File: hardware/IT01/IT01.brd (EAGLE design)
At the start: 23.5 x 23.5 mm, 11 parts

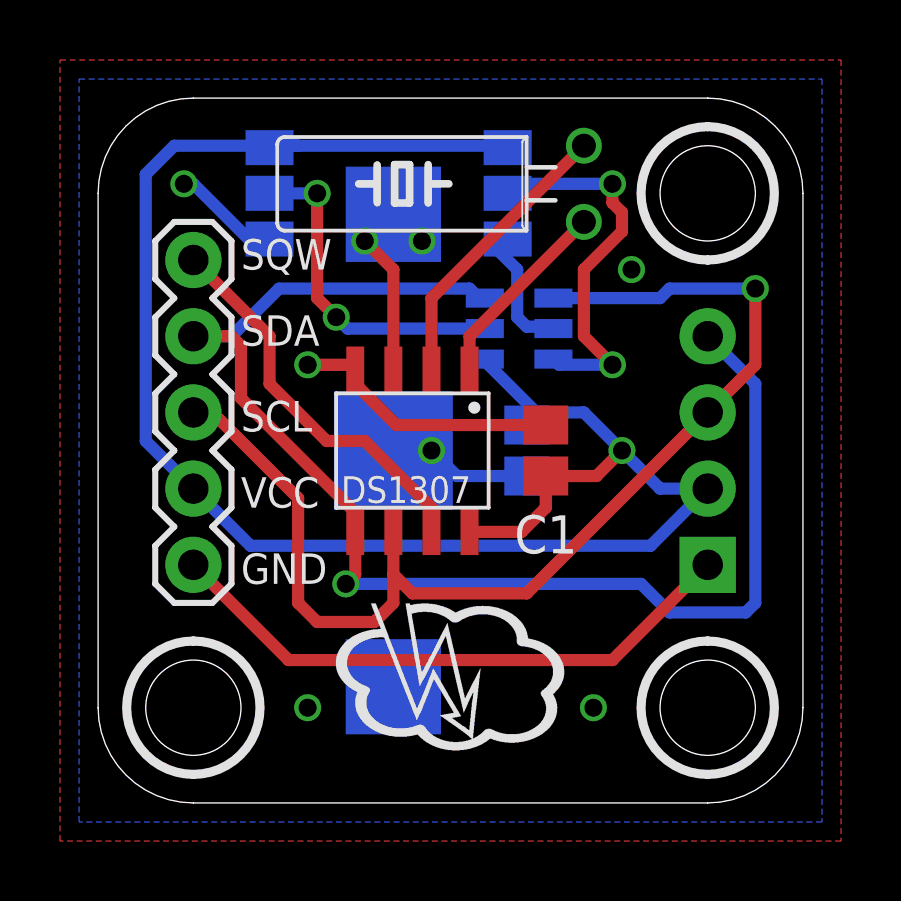
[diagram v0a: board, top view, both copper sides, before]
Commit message: IT01 for Seeedstudio
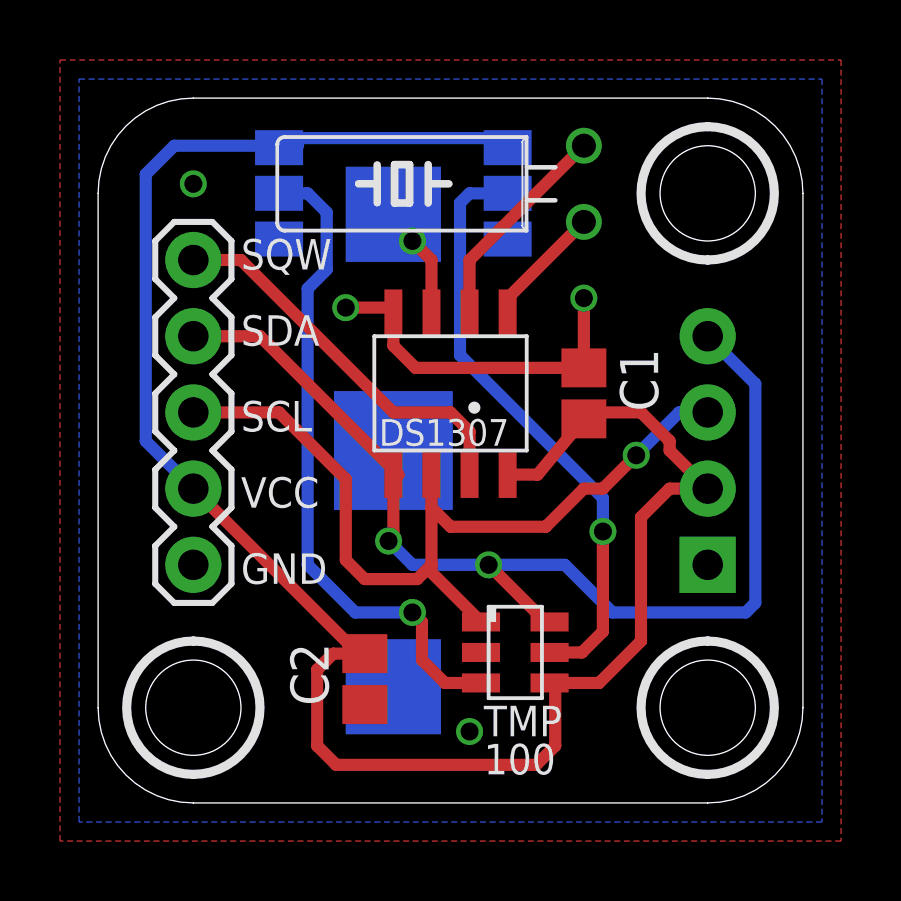
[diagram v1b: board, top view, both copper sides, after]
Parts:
- moved TS1 11.0 mm to (13.0, 7.30), flipped to the top
- moved C2 9.34 mm to (8.89, 4.13), flipped to the top
- moved SJ1 7.94 mm to (13.7, 20.3)
- moved SJ2 7.62 mm to (6.03, 20.3)
- moved DS1307 2.29 mm to (11.7, 13.7)
- moved C1 2.29 mm to (16.2, 13.7)
- moved U$1 1.27 mm to (15.2, 3.81)
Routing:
- net GND: track 40.4 -> 11.7 mm, vias 6 -> 4
- net SCL: track 39.1 -> 28.7 mm
- net AD1: track 12.9 -> 22.0 mm, vias 2 -> 1
- net AD0: track 11.1 -> 20.0 mm, vias 2 -> 1
- net SDA: track 45.6 -> 36.9 mm, vias 1 -> 2
- net VCC: track 61.3 -> 68.4 mm, vias 1 -> 0
- net VBAT: track 12.7 -> 7.37 mm, vias 2 -> 1
- net N$1: track 6.51 -> 4.08 mm
- net N$2: track 9.57 -> 7.14 mm
